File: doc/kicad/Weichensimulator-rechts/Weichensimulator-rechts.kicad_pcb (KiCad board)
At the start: 2 copper layers, 38.1 x 38.1 mm, 9 parts, among them J1 Conn_01x02_Male, J2 Power, J3 Conn_01x02_Male, K1 HFD2_005-S-L2-D

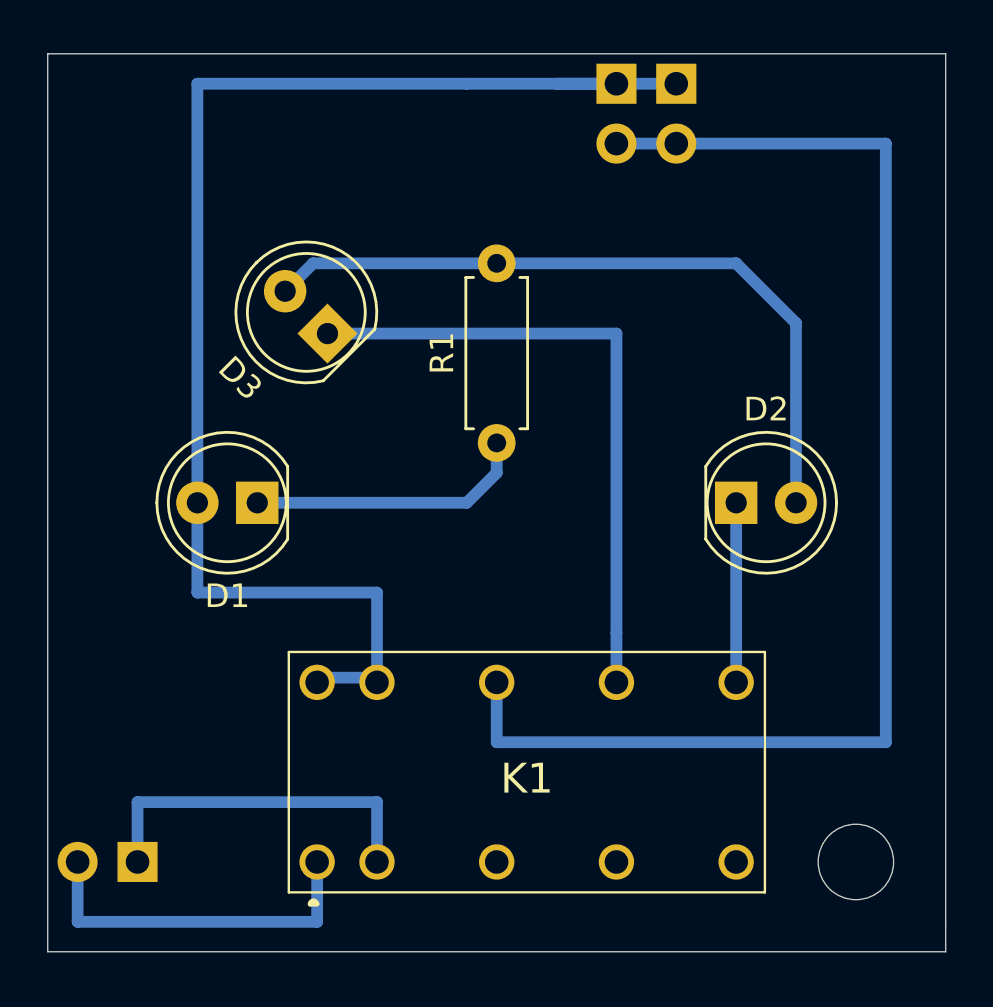
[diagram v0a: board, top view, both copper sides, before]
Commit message: Ecken rund gemacht, alle mit Montagelöcher
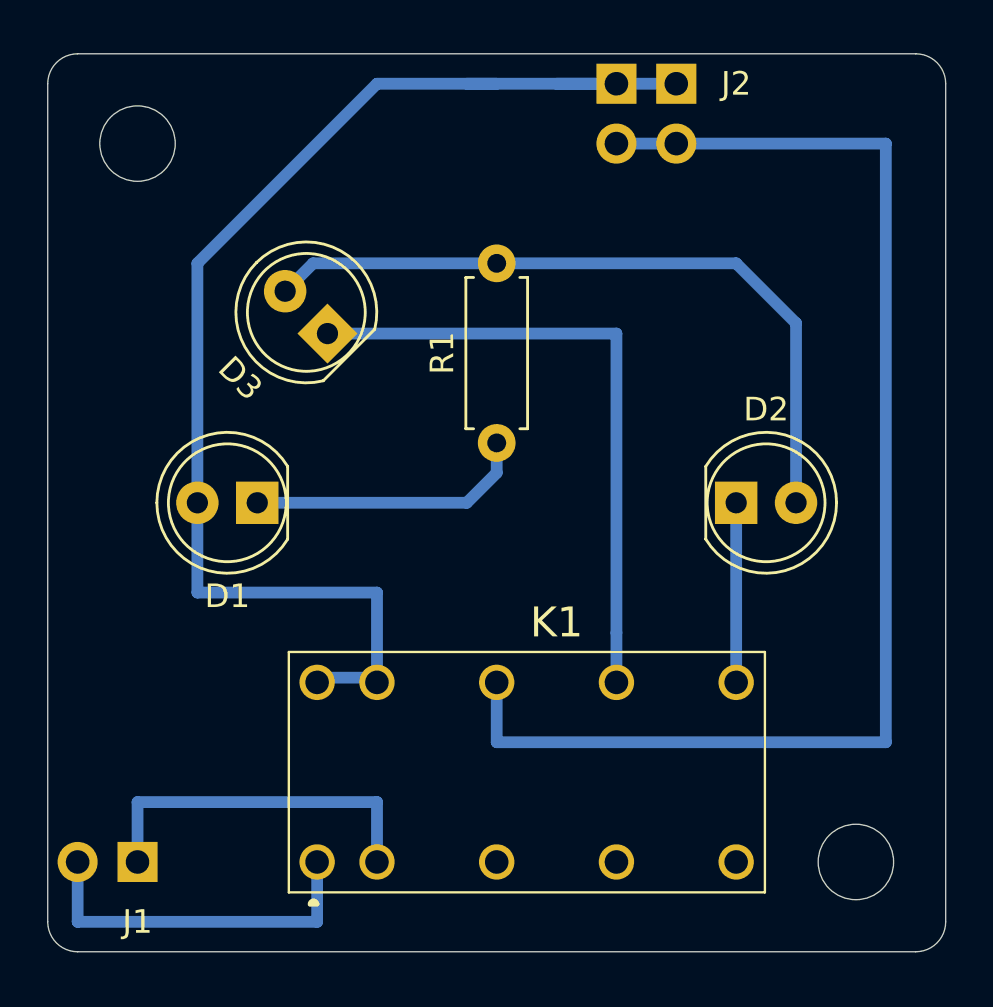
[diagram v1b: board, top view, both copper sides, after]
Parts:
- added H1: MountingHole, Mounting_Holes:MountingHole_3.2mm_M3, F.Cu at (120.7, 92.7)
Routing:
- net +5V: track 58.2 -> 55.0 mm
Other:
- outline, holes or cut-outs redrawn
- board text added: "©H3-H5N6 2021 Weiche re v1.0"

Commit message: Platinen, die an jlcpcb geschickt worden sind.
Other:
- board text added: "A"
- board text added: "G"

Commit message: v2.0 hinzugefügt
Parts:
- K1: moved to B.Cu
- moved D1 20.3 mm to (146.1, 108.0), turned to 0 degrees
- moved D2 20.3 mm to (125.7, 108.0), turned to 180 degrees
- moved K1 15.2 mm to (143.5, 123.2), turned to 180 degrees
- moved R1 9.92 mm to (143.5, 99.1), turned to 180 degrees
- moved J2 5.08 mm to (146.1, 90.2)
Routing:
- net GND: track 55.9 -> 30.0 mm
- net Net-(J1-Pad2): track 15.4 -> 33.3 mm
- net Net-(D3-Pad1): track 27.1 -> 15.7 mm
- net Net-(D2-Pad2): track 30.8 -> 20.5 mm
- net Net-(J1-Pad1): track 15.0 -> 23.9 mm
- net +5V: track 55.0 -> 49.6 mm
- net Net-(D1-Pad1): track 12.0 -> 10.7 mm
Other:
- board text added: "+5V"
- board text added: "GND"
- board text added: "©H3-H5N6 2021 Weiche re v2.0"
- board text removed: "©H3-H5N6 2021 Weiche re v1.0"

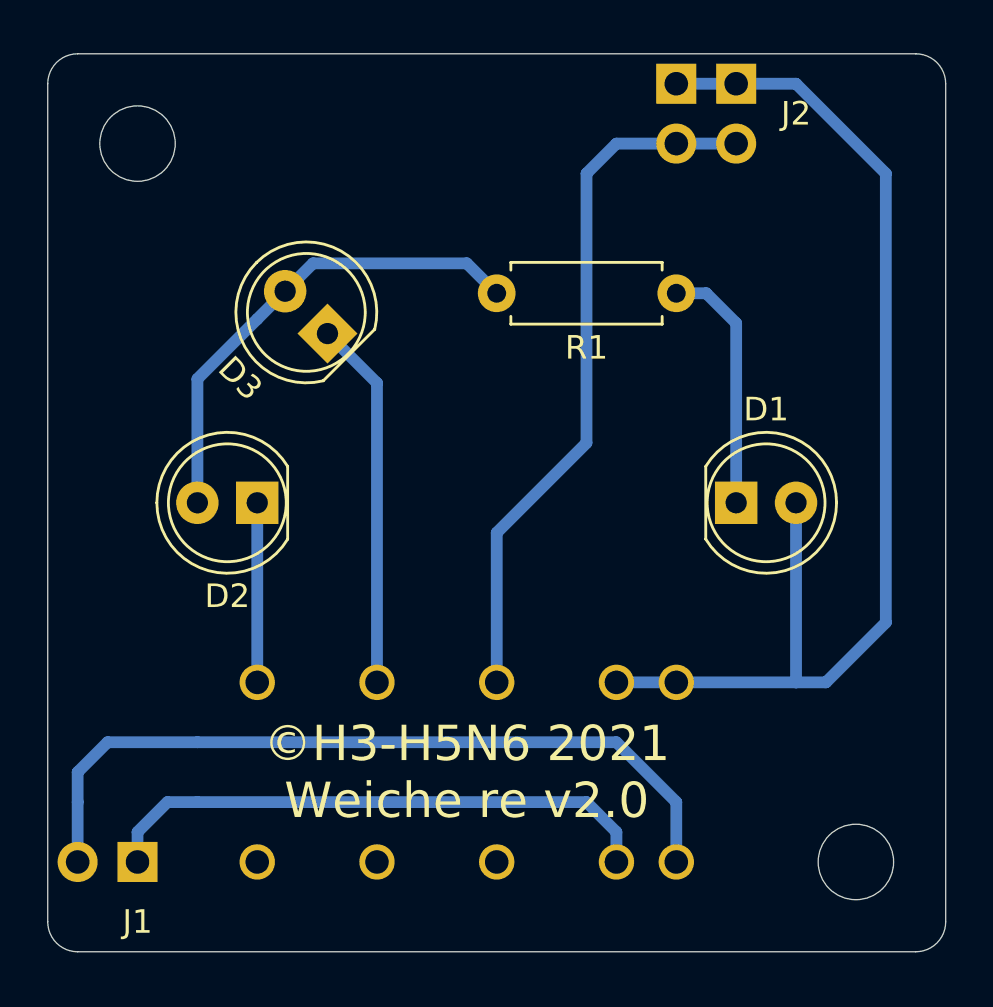
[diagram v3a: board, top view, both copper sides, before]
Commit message: 2. Umschalter herausgeführt
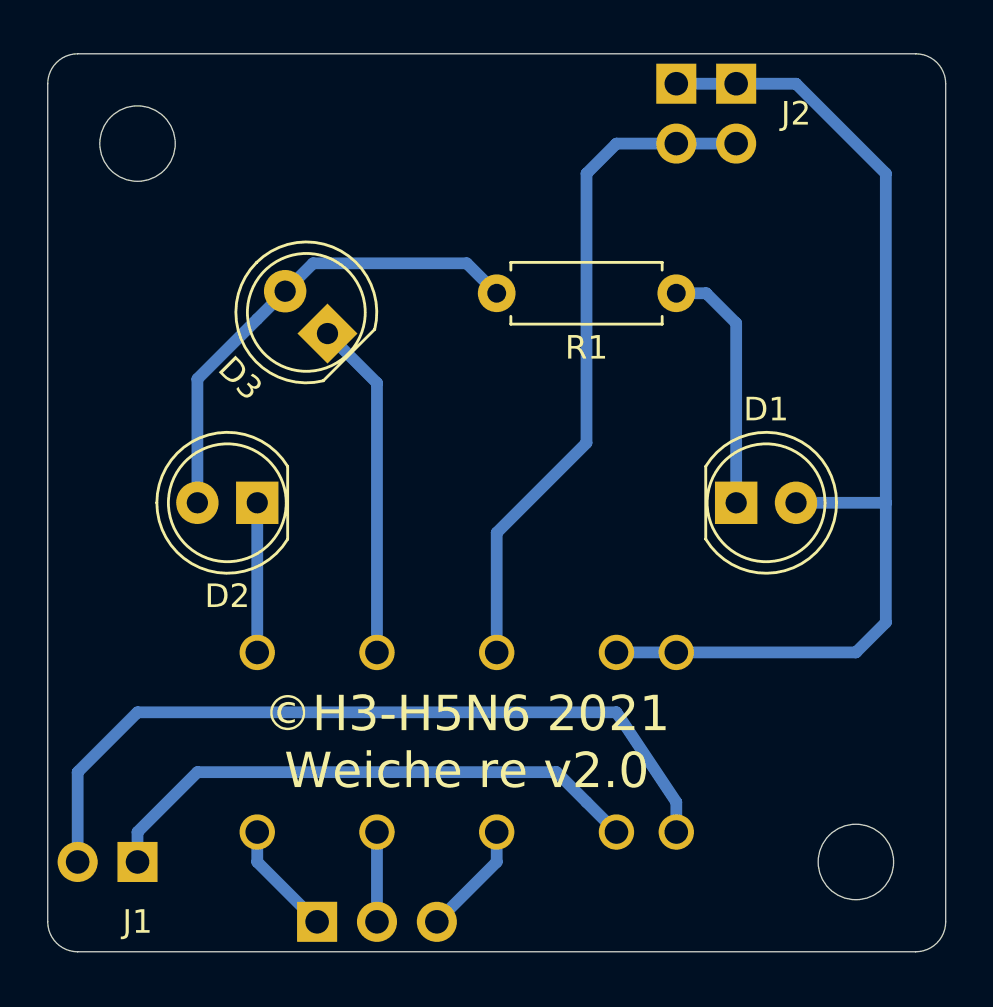
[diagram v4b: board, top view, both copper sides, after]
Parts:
- added Rü1: Conn_01x03_Male, Pin_Headers:Pin_Header_Straight_1x03_Pitch2.54mm, B.Cu at (128.3, 125.7)
- moved K1 1.27 mm to (143.5, 121.9)
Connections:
- K1 pad 4: (no net) -> Net-(K1-Pad4)
- K1 pad 6: (no net) -> Net-(K1-Pad6)
- K1 pad 8: (no net) -> Net-(K1-Pad8)
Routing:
- net Net-(K1-Pad8): track 0.00 -> 4.86 mm
- net Net-(K1-Pad4): track 0.00 -> 4.86 mm
- net +5V: track 49.6 -> 45.3 mm
- net Net-(K1-Pad6): track 0.00 -> 3.81 mm
- net Net-(D3-Pad1): track 15.7 -> 14.4 mm
- net Net-(D2-Pad1): track 7.62 -> 6.35 mm
- net GND: track 30.0 -> 28.8 mm

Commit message: Version 2, jetzt korrekt und auch nutzbar für links, 2. Umschalter herausgeführt
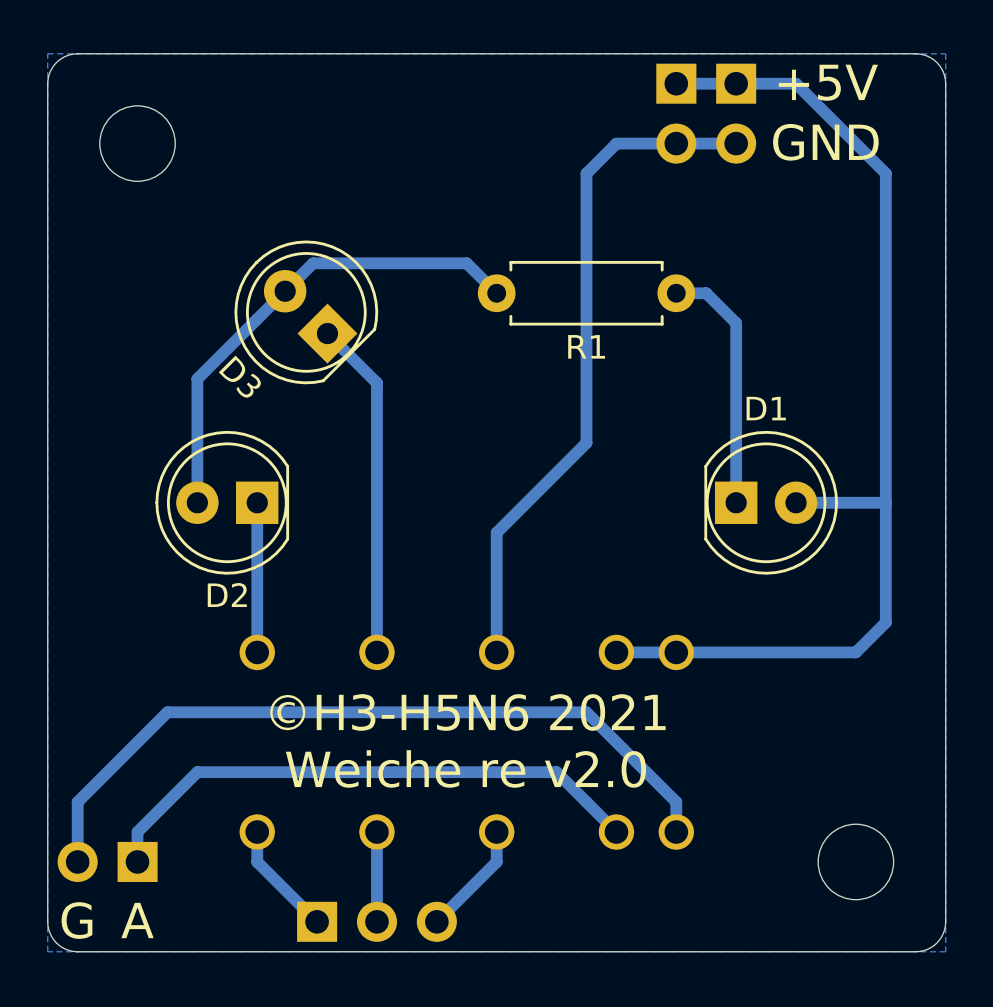
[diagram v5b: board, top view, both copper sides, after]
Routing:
- net Net-(J1-Pad2): track 33.6 -> 32.4 mm
- added copper zone on B.Cu, net (none)
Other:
- board text added: "©H3-H5N6 2021 Weiche li v2.0"
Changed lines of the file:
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@@
   (general
     (thickness 1.6)
-    (drawings 13)
+    (drawings 18)
     (tracks 42)
     (zones 0)
@@
     (descr "Through hole angled pin header, 1x02, 2.54mm pitch, 6mm pin length, single row")
     (tags "Through hole angled pin header THT 1x02 2.54mm single row")
-    (fp_text reference J1 (at -2.54 0 180) (layer F.SilkS)
+    (fp_text reference J1 (at -2.54 0 180) (layer F.SilkS) hide
       (effects (font (size 1 1) (thickness 0.15)))
     )
@@
     (descr "Through hole angled pin header, 1x02, 2.54mm pitch, 6mm pin length, single row")
     (tags "Through hole angled pin header THT 1x02 2.54mm single row")
-    (fp_text reference J2 (at -2.54 -1.27) (layer F.SilkS)
+    (fp_text reference J2 (at -2.54 -1.27) (layer F.SilkS) hide
       (effects (font (size 1 1) (thickness 0.15)))
     )
@@
       (effects (font (size 1 1) (thickness 0.15)) (justify mirror))
     )
-    (fp_text user %R (at 0 -2.54) (layer B.Fab)
-      (effects (font (size 1 1) (thickness 0.15)) (justify mirror))
-    )
     (fp_line (start -0.635 1.27) (end 1.27 1.27) (layer B.Fab) (width 0.1))
     (fp_line (start 1.27 1.27) (end 1.27 -6.35) (layer B.Fab) (width 0.1))
@@
     (fp_line (start 1.8 -6.85) (end 1.8 1.8) (layer B.CrtYd) (width 0.05))
     (fp_line (start 1.8 1.8) (end -1.8 1.8) (layer B.CrtYd) (width 0.05))
+    (fp_text user %R (at 0 -2.54) (layer B.Fab)
+      (effects (font (size 1 1) (thickness 0.15)) (justify mirror))
+    )
     (pad 3 thru_hole oval (at 0 -5.08 270) (size 1.7 1.7) (drill 1) (layers *.Cu *.Mask)
       (net 9 "Net-(K1-Pad4)"))
@@
       (rotate (xyz 0 0 0))
     )
+  )
+  (gr_text G (at 118.11 125.73) (layer F.SilkS)
+    (effects (font (size 1.5 1.5) (thickness 0.3)))
+  )
+  (gr_text A (at 120.65 125.73) (layer F.SilkS)
+    (effects (font (size 1.5 1.5) (thickness 0.3)))
+  )
+  (gr_text GND (at 149.86 92.71) (layer F.SilkS)
+    (effects (font (size 1.5 1.5) (thickness 0.3)))
+  )
+  (gr_text +5V (at 149.86 90.17) (layer F.SilkS)
+    (effects (font (size 1.5 1.5) (thickness 0.3)))
+  )
+  (gr_text "©H3-H5N6 2021\nWeiche li v2.0\n" (at 134.62 118.11) (layer B.SilkS)
+    (effects (font (size 1.5 1.5) (thickness 0.3)) (justify mirror))
   )
   (gr_text GND (at 149.86 92.71) (layer B.SilkS)
@@
   (segment (start 128.71 100.77) (end 130.81 102.87) (width 0.5) (layer B.Cu) (net 3) (status 10))
   (segment (start 130.81 102.87) (end 130.81 114.3) (width 0.5) (layer B.Cu) (net 3) (status 20))
-  (segment (start 143.51 120.65) (end 143.51 121.92) (width 0.5) (layer B.Cu) (net 4) (status 20))
-  (segment (start 140.97 116.84) (end 143.51 120.65) (width 0.5) (layer B.Cu) (net 4))
-  (segment (start 120.65 116.84) (end 140.97 116.84) (width 0.5) (layer B.Cu) (net 4))
-  (segment (start 118.11 119.38) (end 120.65 116.84) (width 0.5) (layer B.Cu) (net 4))
-  (segment (start 118.11 123.19) (end 118.11 119.38) (width 0.5) (layer B.Cu) (net 4) (status 10))
+  (segment (start 139.7 116.84) (end 143.51 120.65) (width 0.5) (layer B.Cu) (net 4))
+  (segment (start 121.92 116.84) (end 139.7 116.84) (width 0.5) (layer B.Cu) (net 4))
+  (segment (start 118.11 120.65) (end 121.92 116.84) (width 0.5) (layer B.Cu) (net 4))
+  (segment (start 143.51 120.65) (end 143.51 121.92) (width 0.5) (layer B.Cu) (net 4))
+  (segment (start 118.11 123.19) (end 118.11 120.65) (width 0.5) (layer B.Cu) (net 4))
+  (segment (start 120.65 123.19) (end 120.65 121.92) (width 0.5) (layer B.Cu) (net 5) (status 10))
+  (segment (start 120.65 121.92) (end 123.19 119.38) (width 0.5) (layer B.Cu) (net 5))
+  (segment (start 123.19 119.38) (end 138.43 119.38) (width 0.5) (layer B.Cu) (net 5))
+  (segment (start 138.43 119.38) (end 139.7 120.65) (width 0.5) (layer B.Cu) (net 5))
   (segment (start 139.7 120.65) (end 140.97 121.92) (width 0.5) (layer B.Cu) (net 5) (status 20))
-  (segment (start 138.43 119.38) (end 139.7 120.65) (width 0.5) (layer B.Cu) (net 5))
-  (segment (start 123.19 119.38) (end 138.43 119.38) (width 0.5) (layer B.Cu) (net 5))
-  (segment (start 120.65 121.92) (end 123.19 119.38) (width 0.5) (layer B.Cu) (net 5))
-  (segment (start 120.65 123.19) (end 120.65 121.92) (width 0.5) (layer B.Cu) (net 5) (status 10))
   (segment (start 148.59 90.17) (end 152.4 93.98) (width 0.5) (layer B.Cu) (net 6))
   (segment (start 143.51 90.17) (end 146.05 90.17) (width 0.5) (layer B.Cu) (net 6) (status 30))
@@
   (segment (start 125.73 123.19) (end 128.27 125.73) (width 0.5) (layer B.Cu) (net 11) (status 20))
   (segment (start 125.73 121.92) (end 125.73 123.19) (width 0.5) (layer B.Cu) (net 11) (status 10))
+  (zone (net 0) (net_name "") (layer B.Cu) (hatch edge 0.508)
+    (connect_pads (clearance 0.508))
+    (min_thickness 0.254)
+    (fill yes (arc_segments 32) (thermal_gap 0.508) (thermal_bridge_width 0.508))
+    (polygon
+      (pts
+        (xy 154.94 127) (xy 116.84 127) (xy 116.84 88.9) (xy 154.94 88.9)
+      )
+    )
+  )
 )

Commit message: Auch die Bedruckung jetzt auf beiden Seiten, Platine jetzt komplett für Links und Rechts
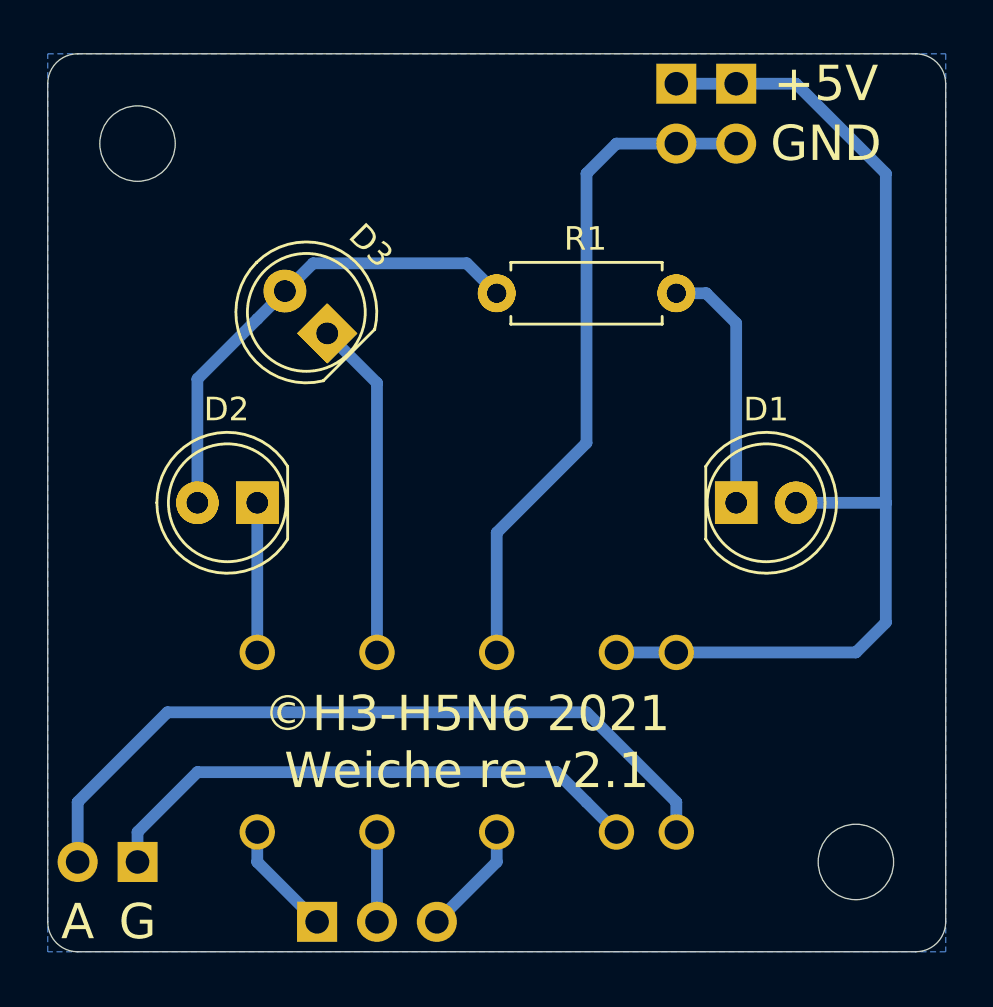
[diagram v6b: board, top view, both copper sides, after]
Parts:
- added D1: LED, LEDs:LED_D5.0mm, B.Cu at (146.1, 108.0)
- added D2: LED, LEDs:LED_D5.0mm, F.Cu at (125.7, 108.0)
- added D3: LED, LEDs:LED_D5.0mm, B.Cu at (128.7, 100.8)
- added R1: 100, Resistors_THT:R_Axial_DIN0207_L6.3mm_D2.5mm_P7.62mm_Horizontal, B.Cu at (143.5, 99.1)
- D2: moved to B.Cu
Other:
- board text added: "©H3-H5N6 2021 Weiche li v2.1"
- board text added: "©H3-H5N6 2021 Weiche re v2.1"
- board text removed: "©H3-H5N6 2021 Weiche li v2.0"
- board text removed: "©H3-H5N6 2021 Weiche re v2.0"

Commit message: Beschriftung für A und G korrigiert, Bauteil-Betruckung auf beiden Seiten
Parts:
- K1: footprint HFD2005SL2D -> HongFa:HFD2005SL2D

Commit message: Aufgeräumt
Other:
- net class Default removed
